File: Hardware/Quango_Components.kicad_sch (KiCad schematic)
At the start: 121 parts, among them J1 Conn_01x12_Male, J2 Conn_01x16_Male, J3 Conn_01x12_Male, J4 Conn_01x12_Male, J5 SWD_Header, J6 Eurorack_10_pin_power, J9 Test_Pin, Q1 MMBT3904, U1 LM1117-3.3, U2 STM32G473V, U3 LM1117-5.0, U4 PS508, U5 MCP6002, U6 AS3364, U7 AS3364, U8 AD5676, U9 MCP48CMB21, Y1 8MHz 20pF

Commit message: Updates to Panel Graphics
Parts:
- removed J3: Conn_01x12_Male, Connector_PinHeader_2.54mm:PinHeader_1x12_P2.54mm_Vertical, symbol Connector:Conn_01x12_Male
- removed J9: Test_Pin, Custom_Footprints:1mm_Test_Point, symbol Connector:Conn_01x01_Female
- added J3: Conn_01x14_Male, Connector_PinHeader_2.54mm:PinHeader_1x14_P2.54mm_Vertical, symbol Connector:Conn_01x14_Male
- U5: footprint Package_SO:MSOP-8_3x3mm_P0.65mm -> Package_SO:SOIC-8_3.9x4.9mm_P1.27mm
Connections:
- net ChannelA_Level: now also J3.11 (Pin_11)
- net ChannelB_Level: now also J3.12 (Pin_12)
- net EnvA1_LED_Out: now also J3.5 (Pin_5)
- net EnvA2_LED_Out: now also J3.4 (Pin_4)
- net EnvA3_LED_Out: now also J3.3 (Pin_3)
- net EnvA4_LED_Out: now also J3.2 (Pin_2)
- net EnvB1_LED_Out: now also J3.8 (Pin_8)
- net EnvB2_LED_Out: now also J3.7 (Pin_7)
- net EnvB3_LED_Out: now also J3.9 (Pin_9)
- net EnvB4_LED_Out: now also J3.6 (Pin_6)
- net GND: now also J3.10 (Pin_10)
- net MIDI_IN: now also J3.1 (Pin_1)
- net Test_Pin2: now reaches U2.81 (PC12)
- net Test_Pin2: now also J3.14 (Pin_14)
- net Test_Pin1: now reaches U2.82 (PD0)
- net Test_Pin1: now also J3.13 (Pin_13)
- no-connect marks 33 -> 32

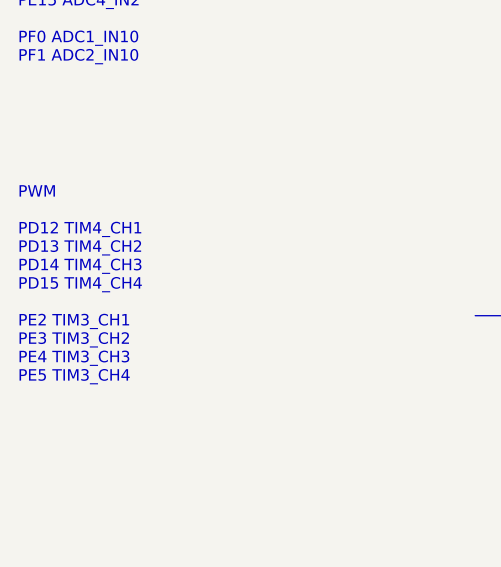
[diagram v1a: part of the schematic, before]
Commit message: Timer 4 PWM Configured and Working
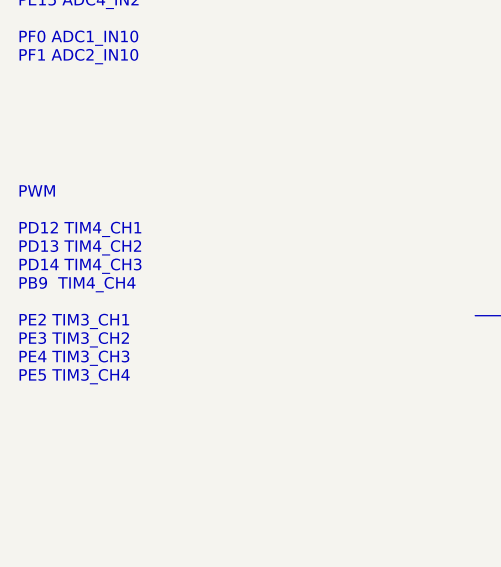
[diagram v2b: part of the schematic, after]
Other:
- note added: "PWM PD12 TIM4_CH1 PD13 TIM4_CH2 PD14 TIM4_CH3 PB9 TIM4_CH4 PE2 TIM3_CH1 PE3 TIM3_CH2 PE4 TIM3_CH3 PE5 TIM3_CH4"
- note removed: "PWM PD12 TIM4_CH1 PD13 TIM4_CH2 PD14 TIM4_CH3 PD15 TIM4_CH4 PE2 TIM3_CH1 PE3 TIM3_CH2 PE4 TIM3_CH3 PE5 TIM3_CH4"
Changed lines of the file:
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@@
     (effects (font (size 1.27 1.27)) (justify left bottom))
   )
-  (text "PWM\n\nPD12 TIM4_CH1\nPD13 TIM4_CH2\nPD14 TIM4_CH3\nPD15 TIM4_CH4\n\nPE2 TIM3_CH1\nPE3 TIM3_CH2\nPE4 TIM3_CH3\nPE5 TIM3_CH4\n"
+  (text "PWM\n\nPD12 TIM4_CH1\nPD13 TIM4_CH2\nPD14 TIM4_CH3\nPB9  TIM4_CH4\n\nPE2 TIM3_CH1\nPE3 TIM3_CH2\nPE4 TIM3_CH3\nPE5 TIM3_CH4\n"
     (at -36.83 193.04 0)
     (effects (font (size 1.27 1.27)) (justify left bottom))

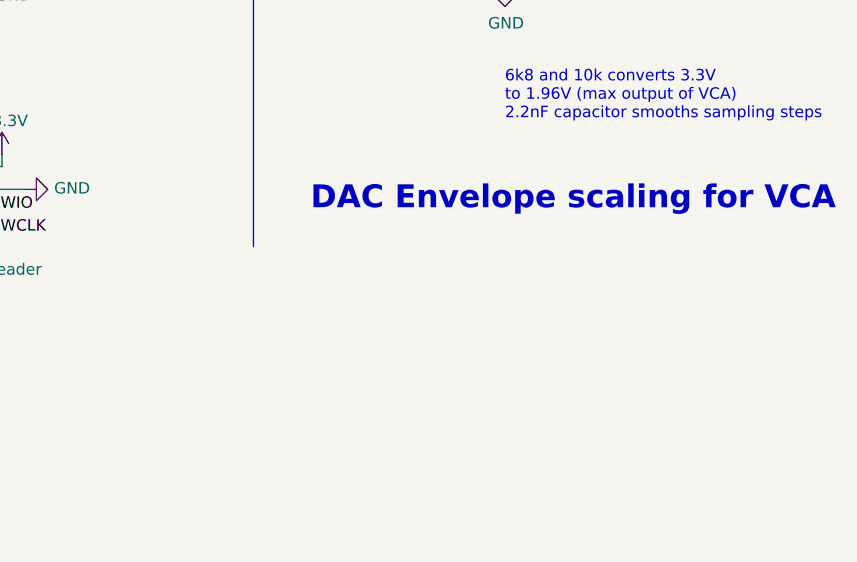
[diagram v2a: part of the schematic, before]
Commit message: Multiplexer tested working; PCB bug - U14 power rails inverted
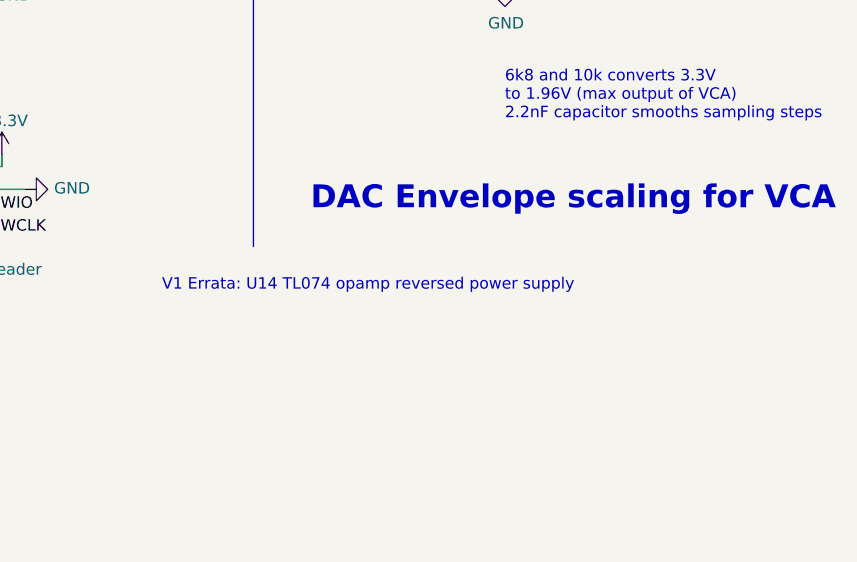
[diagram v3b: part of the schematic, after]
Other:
- note added: "V1 Errata: U14 TL074 opamp reversed power supply"
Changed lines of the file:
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@@
+    (effects (font (size 1.27 1.27)) (justify left bottom))
+  )
+  (text "V1 Errata: U14 TL074 opamp reversed power supply" (at 303.53 256.54 0)
     (effects (font (size 1.27 1.27)) (justify left bottom))
   )

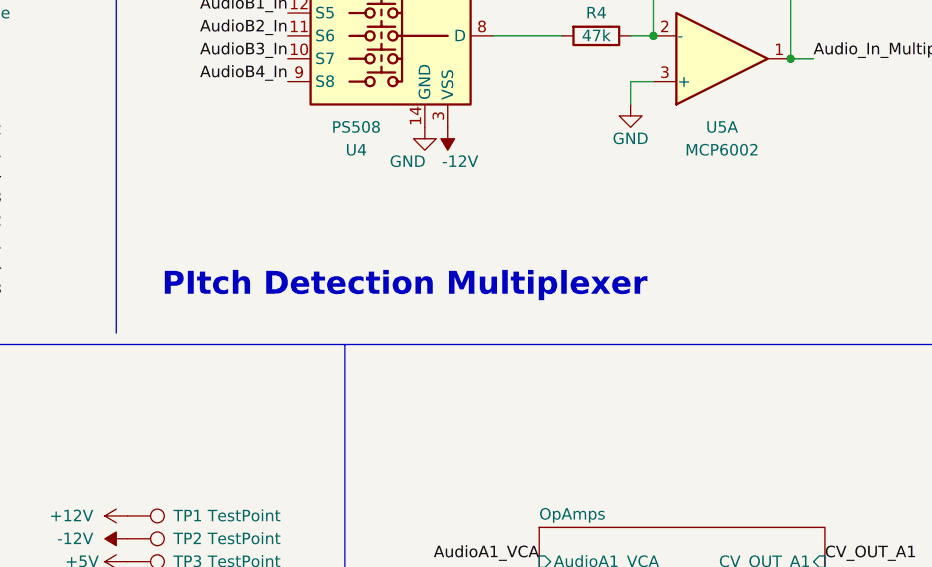
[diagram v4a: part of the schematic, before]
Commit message: Prepared v2 controls and panel for  manufacture
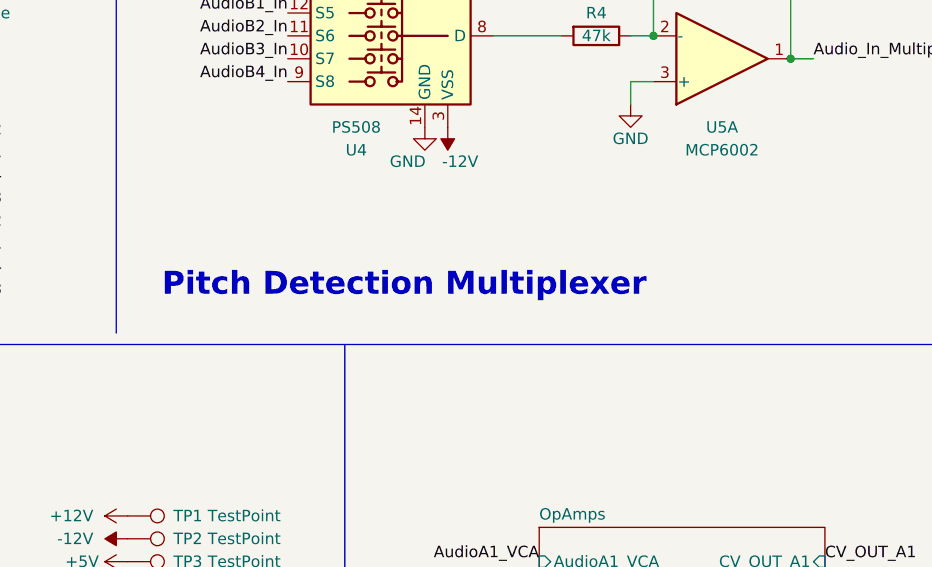
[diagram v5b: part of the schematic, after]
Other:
- note added: "Pitch Detection Multiplexer"
- note removed: "PItch Detection Multiplexer"
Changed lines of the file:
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@@
     (stroke (width 0) (type solid) (color 0 0 0 0))
   )
-  (text "PItch Detection Multiplexer" (at 166.37 180.34 0)
+  (text "Pitch Detection Multiplexer" (at 166.37 180.34 0)
     (effects (font (size 2.54 2.54) (thickness 0.508) bold) (justify left bottom))
   )

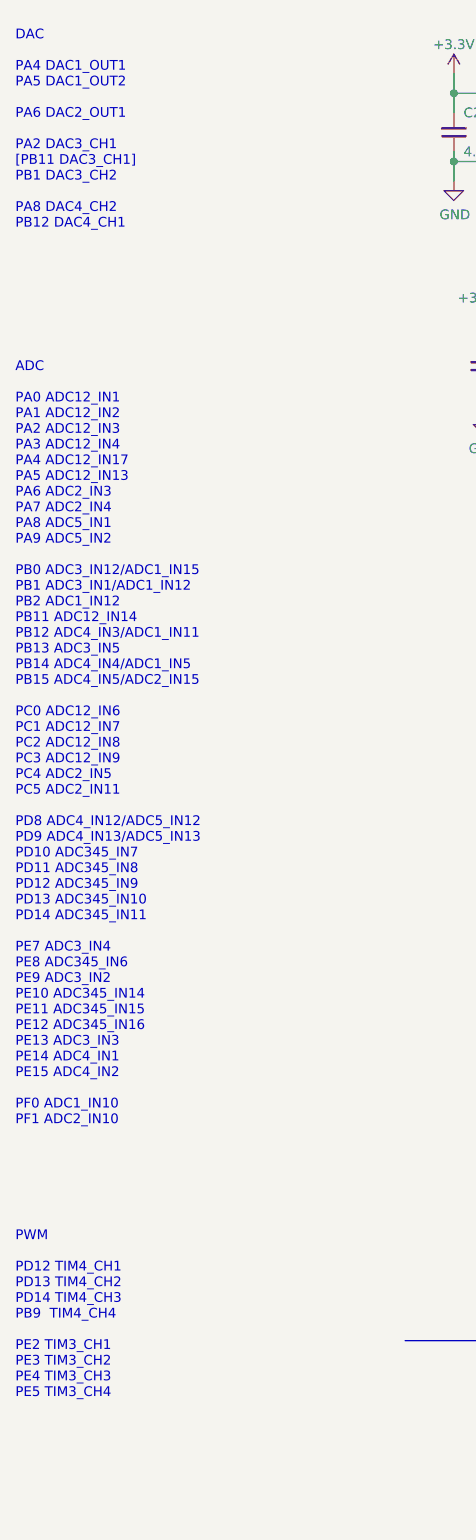
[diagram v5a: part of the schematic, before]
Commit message: Added Breakout gerbers; Added pdfs of schematics
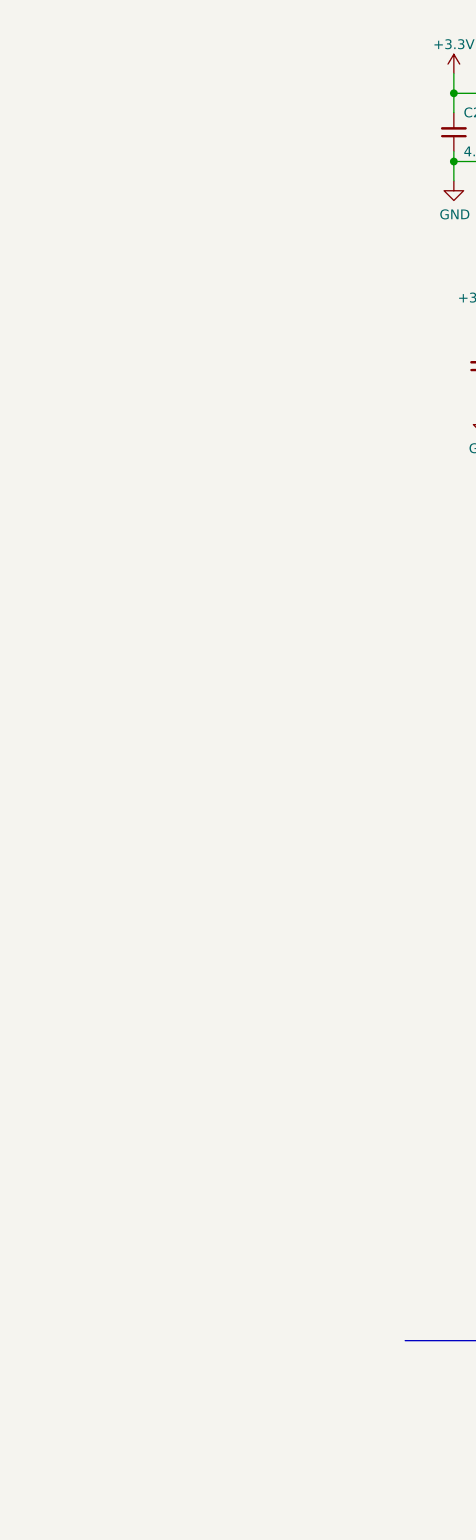
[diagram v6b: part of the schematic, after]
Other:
- note removed: "ADC PA0 ADC12_IN1 PA1 ADC12_IN2 PA2 ADC12_IN3 PA3 ADC12_IN4 PA4 ADC12_IN17 PA5 ADC12_IN13 PA6 ADC2_IN3 PA7 ADC2_IN4 PA8 ADC5_IN1 PA9 ADC5_IN2 PB0 ADC3_IN12/ADC1_IN15 PB1 ADC3_IN1/ADC1_IN12 PB2 ADC1_IN12 PB11 ADC12_IN14 PB12 ADC4_IN3/ADC1_IN11 PB13 ADC3_IN5 PB14 ADC4_IN4/ADC1_IN5 PB15 ADC4_IN5/ADC2_IN15 PC0 ADC12_IN6 PC1 ADC12_IN7 PC2 ADC12_IN8 PC3 ADC12_IN9 PC4 ADC2_IN5 PC5 ADC2_IN11 PD8 ADC4_IN1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"
- note removed: "DAC PA4 DAC1_OUT1 PA5 DAC1_OUT2 PA6 DAC2_OUT1 PA2 DAC3_CH1 [PB11 DAC3_CH1] PB1 DAC3_CH2 PA8 DAC4_CH2 PB12 DAC4_CH1"
- note removed: "PWM PD12 TIM4_CH1 PD13 TIM4_CH2 PD14 TIM4_CH3 PB9 TIM4_CH4 PE2 TIM3_CH1 PE3 TIM3_CH2 PE4 TIM3_CH3 PE5 TIM3_CH4"
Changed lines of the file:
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@@
     (effects (font (size 2.54 2.54) (thickness 0.508) bold) (justify left bottom))
-  )
-  (text "DAC\n\nPA4 DAC1_OUT1\nPA5 DAC1_OUT2\n\nPA6 DAC2_OUT1\n\nPA2 DAC3_CH1\n[PB11 DAC3_CH1]\nPB1 DAC3_CH2\n\nPA8 DAC4_CH2\nPB12 DAC4_CH1\n"
-    (at -36.83 40.64 0)
-    (effects (font (size 1.27 1.27)) (justify left bottom))
   )
   (text "V1 Errata: U14 TL074 opamp reversed power supply" (at 303.53 256.54 0)
@@
     (effects (font (size 1.27 1.27)) (justify left bottom))
   )
-  (text "PWM\n\nPD12 TIM4_CH1\nPD13 TIM4_CH2\nPD14 TIM4_CH3\nPB9  TIM4_CH4\n\nPE2 TIM3_CH1\nPE3 TIM3_CH2\nPE4 TIM3_CH3\nPE5 TIM3_CH4\n"
-    (at -36.83 193.04 0)
-    (effects (font (size 1.27 1.27)) (justify left bottom))
-  )
-  (text "ADC\n\nPA0 ADC12_IN1\nPA1 ADC12_IN2\nPA2 ADC12_IN3\nPA3 ADC12_IN4\nPA4 ADC12_IN17\nPA5 ADC12_IN13\nPA6 ADC2_IN3\nPA7 ADC2_IN4\nPA8 ADC5_IN1\nPA9 ADC5_IN2\n\nPB0 ADC3_IN12/ADC1_IN15\nPB1 ADC3_IN1/ADC1_IN12\nPB2 ADC1_IN12\nPB11 ADC12_IN14\nPB12 ADC4_IN3/ADC1_IN11\nPB13 ADC3_IN5\nPB14 ADC4_IN4/ADC1_IN5\nPB15 ADC4_IN5/ADC2_IN15\n\nPC0 ADC12_IN6\nPC1 ADC12_IN7\nPC2 ADC12_IN8\nPC3 ADC12_IN9\nPC4 ADC2_IN5\nPC5 ADC2_IN11\n\nPD8 ADC4_IN12/ADC5_IN12\nPD9 ADC4_IN13/ADC5_IN13\nPD10 ADC345_IN7\nPD11 ADC345_IN8\nPD12 ADC345_IN9\nPD13 ADC345_IN10\nPD14 ADC345_IN11\n\nPE7 ADC3_IN4\nPE8 ADC345_IN6\nPE9 ADC3_IN2\nPE10 ADC345_IN14\nPE11 ADC345_IN15\nPE12 ADC345_IN16\nPE13 ADC3_IN3\nPE14 ADC4_IN1\nPE15 ADC4_IN2\n\nPF0 ADC1_IN10\nPF1 ADC2_IN10"
-    (at -36.83 157.48 0)
-    (effects (font (size 1.27 1.27)) (justify left bottom))
-  )

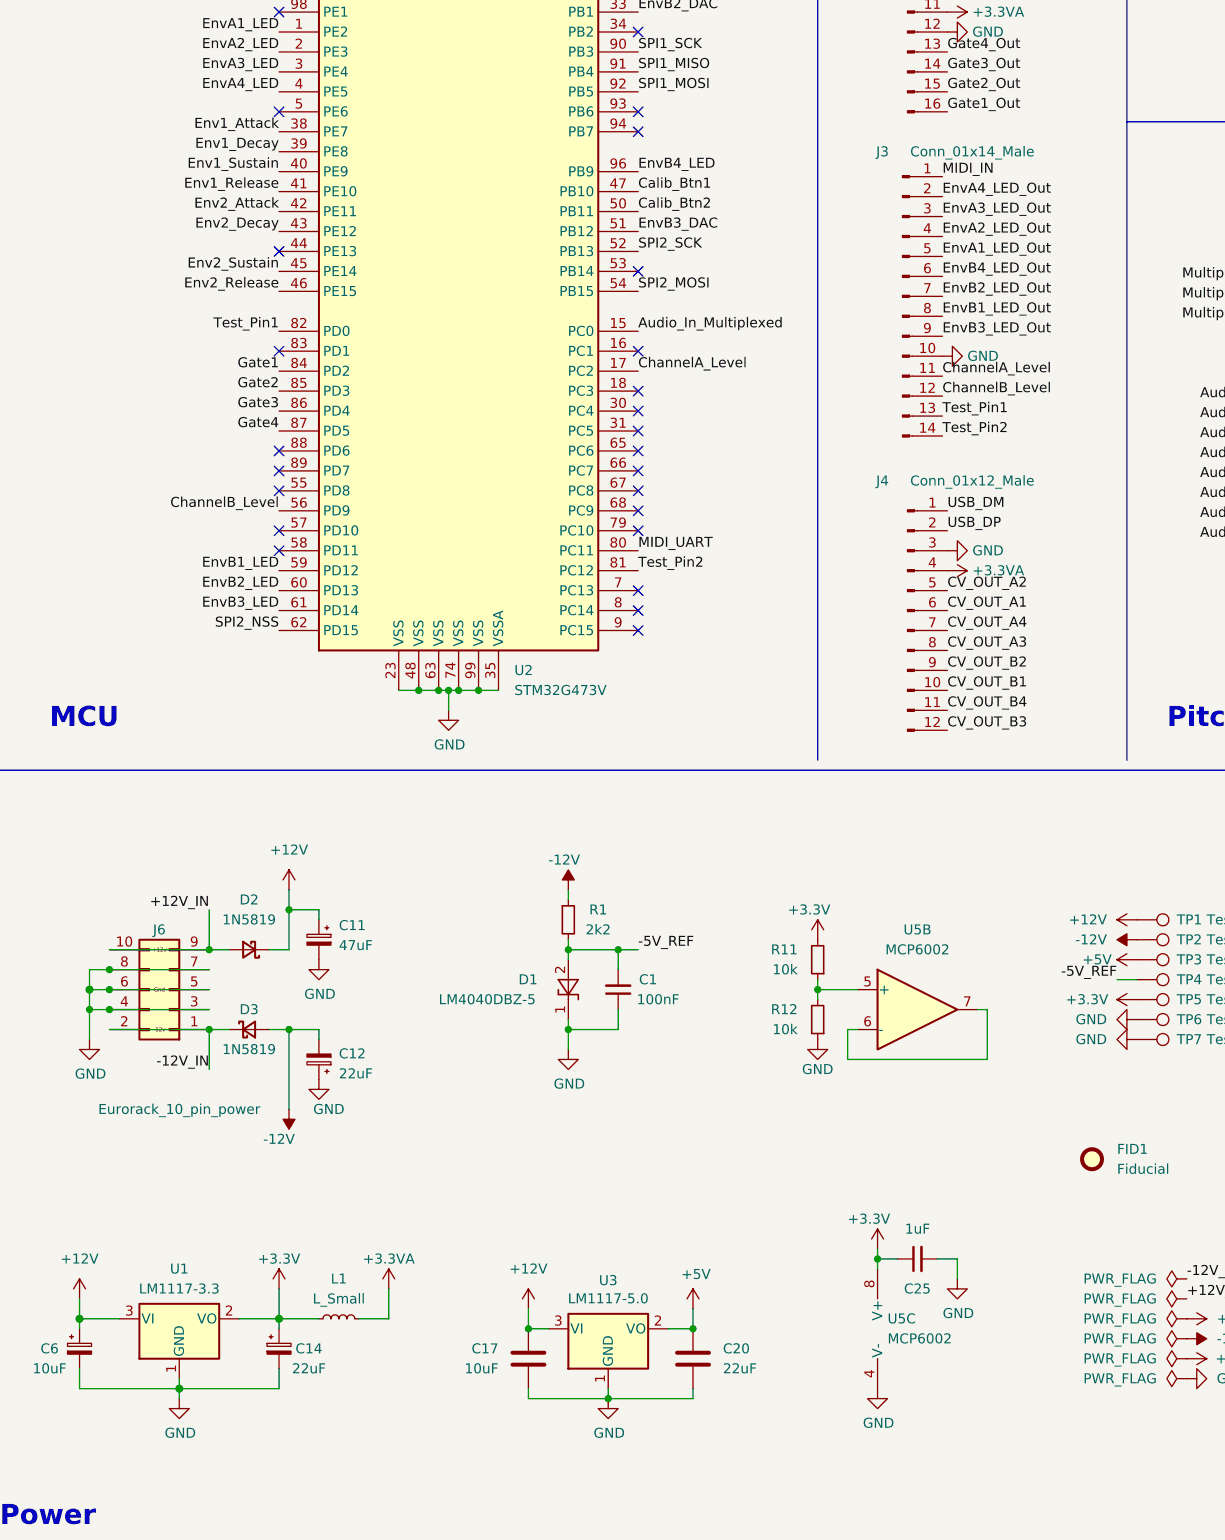
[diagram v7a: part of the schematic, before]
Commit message: Updated component schematic/pcb to v2
Kicad 8.0
Fixing opamp U14 power reversal
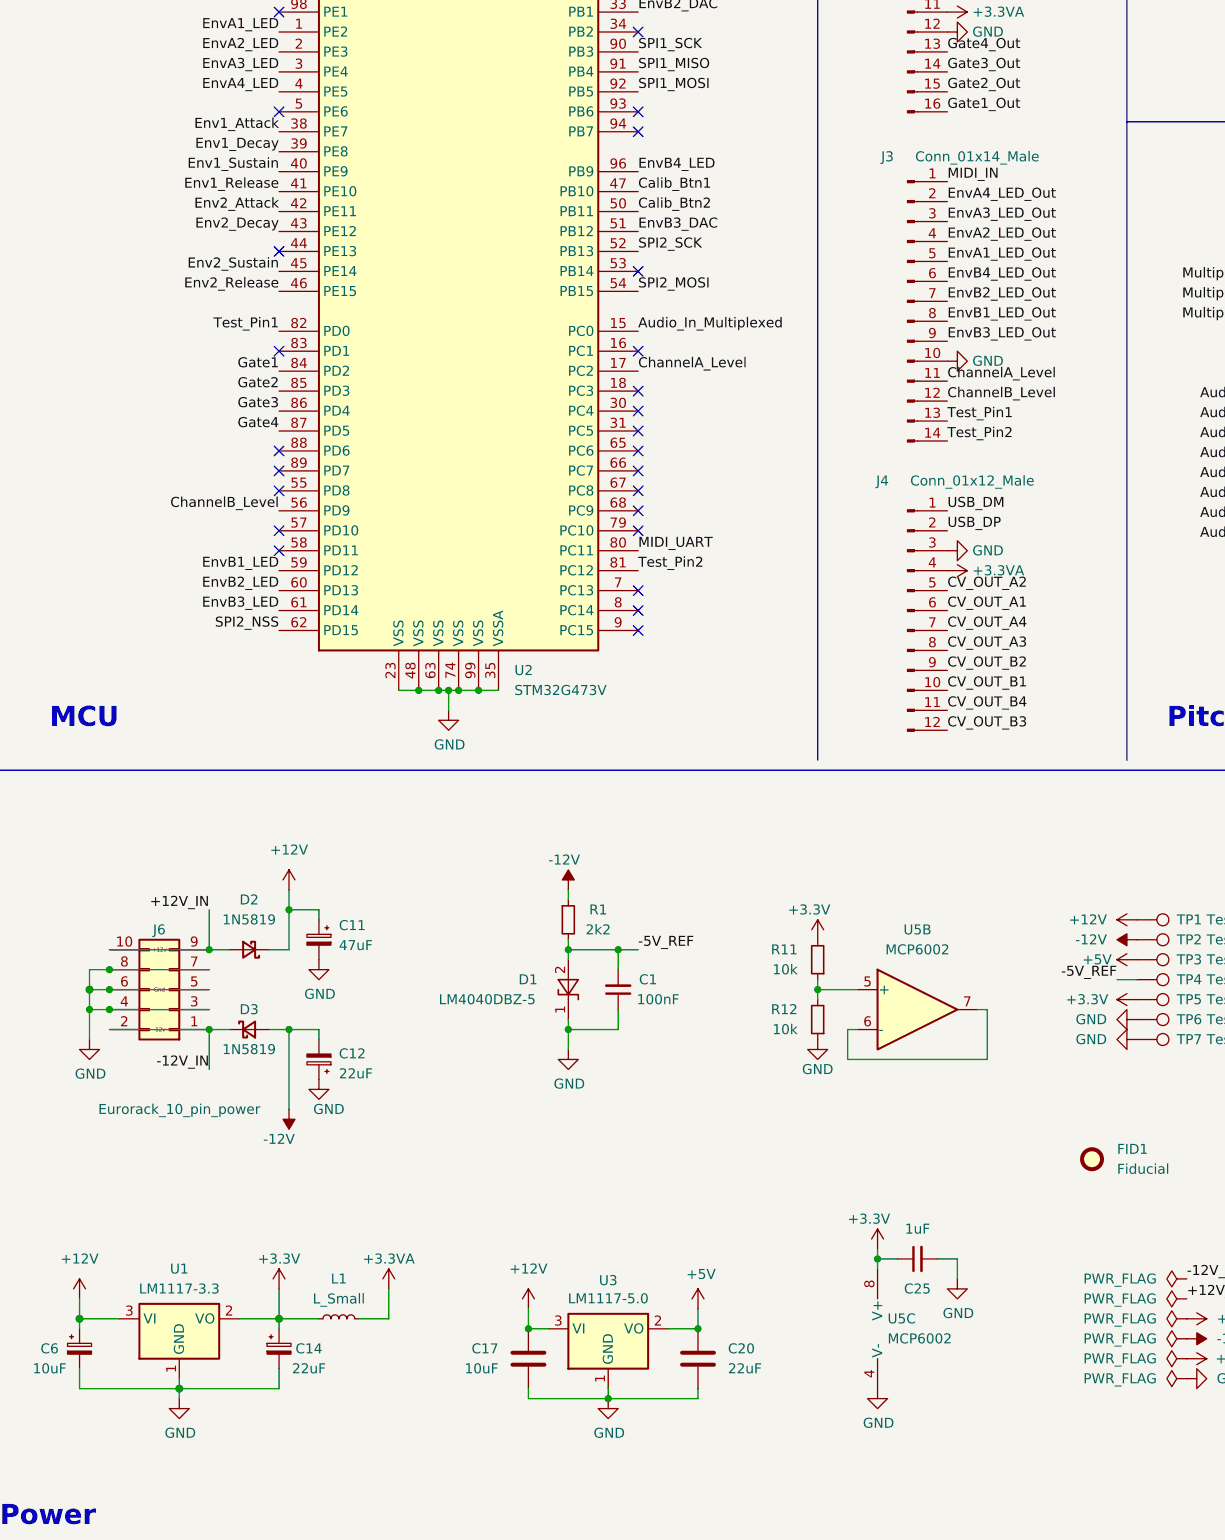
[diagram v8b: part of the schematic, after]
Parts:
- C11, C12, C14, C6: symbol Encoder:CP_Small -> Device:C_Polarized_Small
- J1, J4: symbol Connector:Conn_01x12_Male -> Connector:Conn_01x12_Pin
- J2: symbol Connector:Conn_01x16_Male -> Connector:Conn_01x16_Pin
- J3: symbol Connector:Conn_01x14_Male -> Connector:Conn_01x14_Pin
- J5: symbol Connector:Conn_01x04_Male -> Connector:Conn_01x04_Pin
- U1: symbol Regulator_Linear:LM1117-3.3 -> Regulator_Linear:LM1117MP-3.3
- U3: symbol Regulator_Linear:LM1117-5.0 -> Regulator_Linear:LM1117MP-5.0
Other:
- moved on the sheet: C20, J3
